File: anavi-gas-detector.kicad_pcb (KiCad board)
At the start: 2 copper layers, 74.9 x 40.6 mm, 29 parts, among them P1 CONN_01X03, U1 I2C_SENS_1, U2 I2C_SENS_1, U3 I2C_SENS_1

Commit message: anavi-gas-detector.kicad_pcb: Update labels
Improve the labels.

Signed-off-by: Leon Anavi <leon@anavi.org>
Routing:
- net +3V3: track 122.7 -> 118.7 mm, vias 2 -> 0
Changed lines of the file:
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@@
     (thickness 1.6)
     (drawings 22)
-    (tracks 187)
+    (tracks 184)
     (zones 0)
     (modules 29)
@@
       (drillshape 0)
       (scaleselection 1)
-      (outputdirectory "plots/anavi-thermometer-r1.0/"))
+      (outputdirectory "plots/anavi-gas-detector-r1.0/"))
   )
   (net 0 "")
@@
     (tags diode)
     (attr smd)
-    (fp_text reference D2 (at 0 -2.032 180) (layer F.SilkS)
+    (fp_text reference D2 (at 0 -2.1209 180) (layer F.SilkS)
       (effects (font (size 1 1) (thickness 0.15)))
     )
@@
     (tags diode)
     (attr smd)
-    (fp_text reference D3 (at 0 -1.905 180) (layer F.SilkS)
+    (fp_text reference D3 (at 0 -2.159 180) (layer F.SilkS)
       (effects (font (size 1 1) (thickness 0.15)))
     )
@@
     (tags diode)
     (attr smd)
-    (fp_text reference D4 (at 0.0635 -1.905 180) (layer F.SilkS)
+    (fp_text reference D4 (at 0 -2.1336 180) (layer F.SilkS)
       (effects (font (size 1 1) (thickness 0.15)))
     )
@@
     (tags resistor)
     (attr smd)
-    (fp_text reference R5 (at 0 -1.43) (layer F.SilkS)
+    (fp_text reference R5 (at 0.0128 1.6129) (layer F.SilkS)
       (effects (font (size 0.8 0.8) (thickness 0.1)))
     )
-    (fp_text value 68R (at 0 1.43) (layer F.Fab)
+    (fp_text value 68R (at 0 -1.4605) (layer F.Fab)
       (effects (font (size 1 1) (thickness 0.15)))
     )
@@
     (tags resistor)
     (attr smd)
-    (fp_text reference R6 (at 0 -1.43) (layer F.SilkS)
+    (fp_text reference R6 (at -0.0126 1.4986) (layer F.SilkS)
       (effects (font (size 0.8 0.8) (thickness 0.1)))
     )
-    (fp_text value 68R (at 0 1.43) (layer F.Fab)
+    (fp_text value 68R (at 0.1398 -1.3716) (layer F.Fab)
       (effects (font (size 1 1) (thickness 0.15)))
     )
@@
     (tags resistor)
     (attr smd)
-    (fp_text reference R7 (at 0 -1.43) (layer F.SilkS)
+    (fp_text reference R7 (at 0.0127 1.5494) (layer F.SilkS)
       (effects (font (size 0.8 0.8) (thickness 0.1)))
     )
-    (fp_text value 68R (at 0 1.43) (layer F.Fab)
+    (fp_text value 68R (at 0.0381 -1.3716) (layer F.Fab)
       (effects (font (size 1 1) (thickness 0.15)))
     )
@@
     (descr "Through hole straight pin header, 1x04, 2.54mm pitch, single row")
     (tags "Through hole pin header THT 1x04 2.54mm single row")
-    (fp_text reference GPIO (at 0 -2.667 270) (layer F.SilkS)
-      (effects (font (size 0.8 0.8) (thickness 0.1)))
+    (fp_text reference GPIO (at 0 -2.9718 270) (layer F.SilkS)
+      (effects (font (size 1 1) (thickness 0.2)))
     )
     (fp_text value Conn_01x04 (at 0 9.95 270) (layer F.Fab) hide
@@
     (effects (font (size 1 1) (thickness 0.2)))
   )
-  (gr_text "3 x I2C" (at 98.044 90.17 90) (layer F.SilkS)
-    (effects (font (size 1 1) (thickness 0.2)))
+  (gr_text "3 x I2C" (at 111.5822 90.297 90) (layer F.SilkS)
+    (effects (font (size 1.5 1.5) (thickness 0.25)))
   )
   (gr_line (start 69.85 71.12) (end 134.62 71.12) (angle 90) (layer Edge.Cuts) (width 0.15))
@@
   (segment (start 108.3945 90.297) (end 108.3945 91.813) (width 0.5) (layer F.Cu) (net 3))
   (segment (start 108.3945 95.5294) (end 108.3945 95.377) (width 0.5) (layer F.Cu) (net 3))
-  (via (at 80.264 101.6) (size 0.85) (drill 0.4) (layers F.Cu B.Cu) (net 3))
   (segment (start 78.283 99.568) (end 78.283 99.619) (width 0.5) (layer F.Cu) (net 3))
-  (segment (start 78.283 99.619) (end 80.264 101.6) (width 0.5) (layer F.Cu) (net 3))
-  (via (at 80.264 97.028) (size 0.85) (drill 0.4) (layers F.Cu B.Cu) (net 3))
-  (segment (start 80.264 101.6) (end 80.264 97.028) (width 0.5) (layer B.Cu) (net 3))
-  (segment (start 80.264 94.645) (end 80.899 94.01) (width 0.5) (layer F.Cu) (net 3))
-  (segment (start 80.264 97.028) (end 80.264 94.645) (width 0.5) (layer F.Cu) (net 3))
   (segment (start 80.899 84.01) (end 88.582 84.01) (width 0.5) (layer F.Cu) (net 3))
   (segment (start 88.582 84.01) (end 90.678 86.106) (width 0.5) (layer F.Cu) (net 3))
@@
   (segment (start 117.745022 81.6864) (end 122.682 76.749422) (width 0.5) (layer F.Cu) (net 3))
   (segment (start 113.2887 81.6864) (end 117.745022 81.6864) (width 0.5) (layer F.Cu) (net 3))
+  (segment (start 78.744612 99.106388) (end 78.744612 96.164388) (width 0.5) (layer F.Cu) (net 3))
+  (segment (start 78.744612 96.164388) (end 80.899 94.01) (width 0.5) (layer F.Cu) (net 3))
+  (segment (start 78.283 99.568) (end 78.744612 99.106388) (width 0.5) (layer F.Cu) (net 3))
   (segment (start 100.5635 95.969) (end 100.7745 95.758) (width 0.5) (layer F.Cu) (net 4))
   (segment (start 100.754 85.1965) (end 100.7745 85.217) (width 0.5) (layer F.Cu) (net 4))

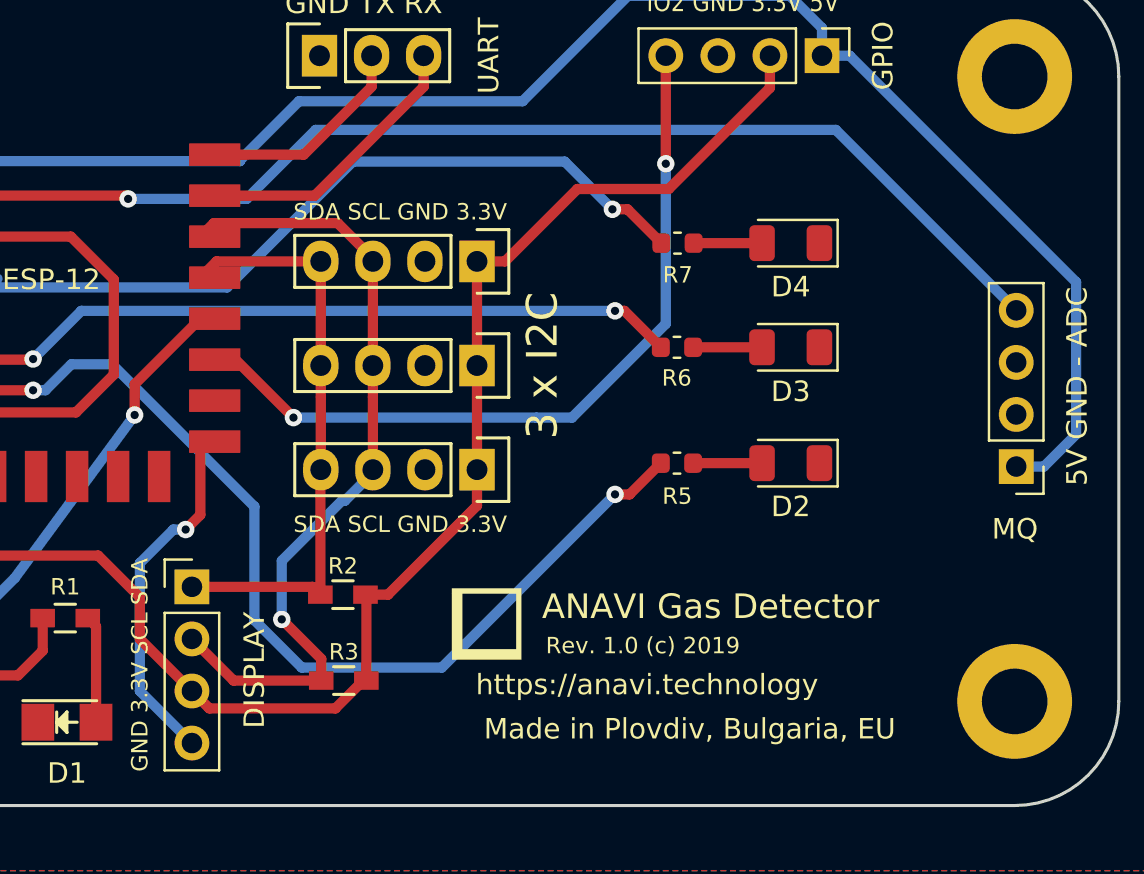
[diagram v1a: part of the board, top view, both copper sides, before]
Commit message: anavi-gas-detector.*: Add voltage dividers
Add voltage divider to measure accrately the analog
output from the external gas sensor.

Signed-off-by: Leon Anavi <leon@anavi.org>
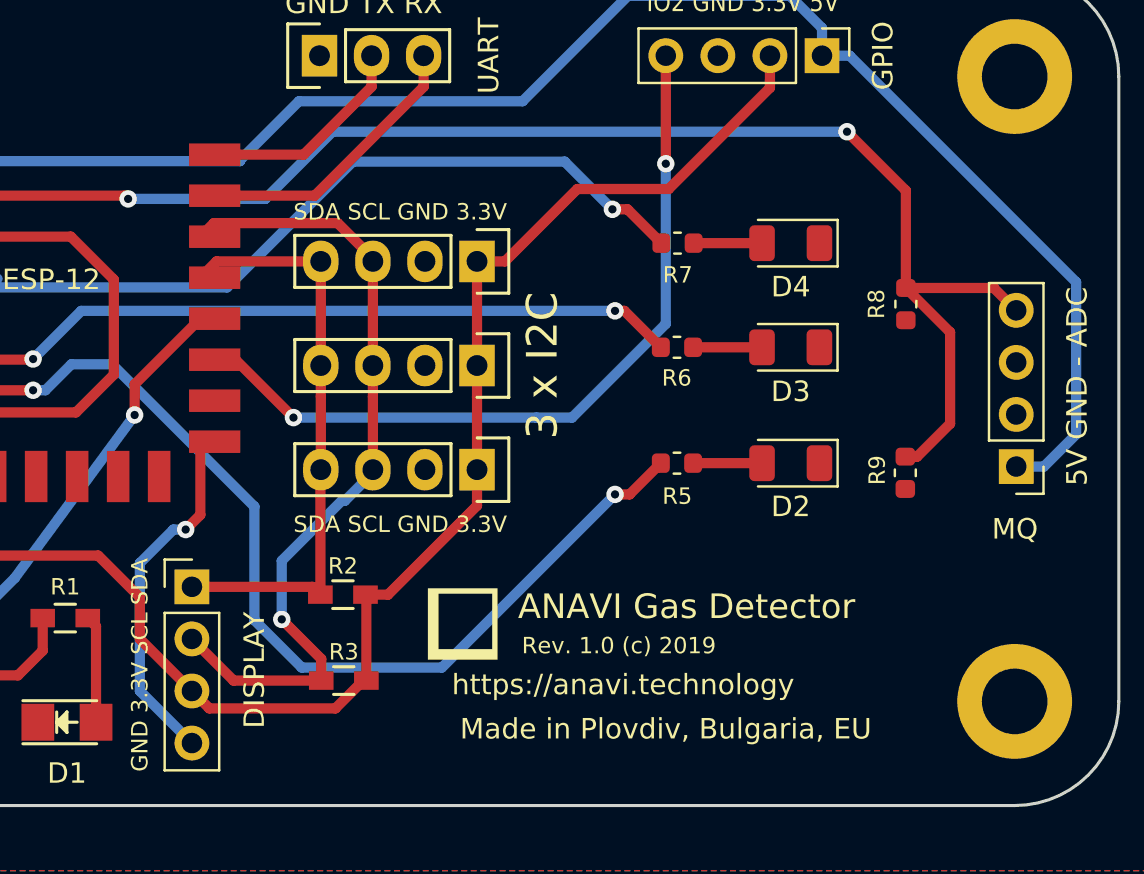
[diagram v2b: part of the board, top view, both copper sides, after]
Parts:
- added R8: 220K, Resistor_SMD:R_0603_1608Metric, F.Cu at (129.3, 87.3)
- added R9: 56K, Resistor_SMD:R_0603_1608Metric, F.Cu at (129.3, 95.5)
- moved G*** 1.17 mm to (107.7, 102.9)
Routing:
- net Net-(ESP-12-Pad2): track 58.9 -> 72.0 mm, vias 1 -> 2
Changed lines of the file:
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@@
     (thickness 1.6)
     (drawings 22)
-    (tracks 184)
+    (tracks 192)
     (zones 0)
-    (modules 29)
-    (nets 27)
+    (modules 31)
+    (nets 28)
   )
   (page A4)
@@
   (net 25 "Net-(ESP-12-Pad22)")
   (net 26 "Net-(U5-Pad3)")
+  (net 27 "Net-(R8-Pad1)")
   (net_class Default "This is the default net class."
     (clearance 0.254)
@@
     (add_net "Net-(ESP-12-Pad6)")
     (add_net "Net-(ESP-12-Pad7)")
+    (add_net "Net-(R8-Pad1)")
     (add_net "Net-(U5-Pad3)")
   )
@@
   )
   (module logo:anavi-logo (layer F.Cu)
-    (at 108.8644 102.9462)
+    (at 107.696 102.9462)
     (fp_text reference G*** (at 0 0) (layer F.SilkS) hide
       (effects (font (size 1.524 1.524) (thickness 0.3)))
@@
     )
   )
+  (module Resistor_SMD:R_0603_1608Metric (layer F.Cu)
+    (at 129.3114 87.2997 90)
+    (descr "Resistor SMD 0603 (1608 Metric), square (rectangular) end terminal, IPC_7351 nominal, (Body size source: http://www.tortai-tech.com/upload/download/2011102023233369053.pdf), generated with kicad-footprint-generator")
+    (tags resistor)
+    (attr smd)
+    (fp_text reference R8 (at 0 -1.43 90) (layer F.SilkS)
+      (effects (font (size 0.8 0.8) (thickness 0.1)))
+    )
+    (fp_text value 220K (at -0.0255 1.6002 90) (layer F.Fab)
+      (effects (font (size 1 1) (thickness 0.15)))
+    )
+    (fp_text user %R (at 0 0 90) (layer F.Fab)
+      (effects (font (size 0.4 0.4) (thickness 0.06)))
+    )
+    (fp_line (start 1.48 0.73) (end -1.48 0.73) (layer F.CrtYd) (width 0.05))
+    (fp_line (start 1.48 -0.73) (end 1.48 0.73) (layer F.CrtYd) (width 0.05))
+    (fp_line (start -1.48 -0.73) (end 1.48 -0.73) (layer F.CrtYd) (width 0.05))
+    (fp_line (start -1.48 0.73) (end -1.48 -0.73) (layer F.CrtYd) (width 0.05))
+    (fp_line (start -0.162779 0.51) (end 0.162779 0.51) (layer F.SilkS) (width 0.12))
+    (fp_line (start -0.162779 -0.51) (end 0.162779 -0.51) (layer F.SilkS) (width 0.12))
+    (fp_line (start 0.8 0.4) (end -0.8 0.4) (layer F.Fab) (width 0.1))
+    (fp_line (start 0.8 -0.4) (end 0.8 0.4) (layer F.Fab) (width 0.1))
+    (fp_line (start -0.8 -0.4) (end 0.8 -0.4) (layer F.Fab) (width 0.1))
+    (fp_line (start -0.8 0.4) (end -0.8 -0.4) (layer F.Fab) (width 0.1))
+    (pad 2 smd roundrect (at 0.7875 0 90) (size 0.875 0.95) (layers F.Cu F.Paste F.Mask) (roundrect_rratio 0.25)
+      (net 17 "Net-(ESP-12-Pad2)"))
+    (pad 1 smd roundrect (at -0.7875 0 90) (size 0.875 0.95) (layers F.Cu F.Paste F.Mask) (roundrect_rratio 0.25)
+      (net 27 "Net-(R8-Pad1)"))
+    (model ${KISYS3DMOD}/Resistor_SMD.3dshapes/R_0603_1608Metric.wrl
+      (at (xyz 0 0 0))
+      (scale (xyz 1 1 1))
+      (rotate (xyz 0 0 0))
+    )
+  )
+  (module Resistor_SMD:R_0603_1608Metric (layer F.Cu)
+    (at 129.286 95.5295 270)
+    (descr "Resistor SMD 0603 (1608 Metric), square (rectangular) end terminal, IPC_7351 nominal, (Body size source: http://www.tortai-tech.com/upload/download/2011102023233369053.pdf), generated with kicad-footprint-generator")
+    (tags resistor)
+    (attr smd)
+    (fp_text reference R9 (at -0.1271 1.3716 270) (layer F.SilkS)
+      (effects (font (size 0.8 0.8) (thickness 0.1)))
+    )
+    (fp_text value 56K (at 0.0253 -1.5748 270) (layer F.Fab)
+      (effects (font (size 1 1) (thickness 0.15)))
+    )
+    (fp_line (start -0.8 0.4) (end -0.8 -0.4) (layer F.Fab) (width 0.1))
+    (fp_line (start -0.8 -0.4) (end 0.8 -0.4) (layer F.Fab) (width 0.1))
+    (fp_line (start 0.8 -0.4) (end 0.8 0.4) (layer F.Fab) (width 0.1))
+    (fp_line (start 0.8 0.4) (end -0.8 0.4) (layer F.Fab) (width 0.1))
+    (fp_line (start -0.162779 -0.51) (end 0.162779 -0.51) (layer F.SilkS) (width 0.12))
+    (fp_line (start -0.162779 0.51) (end 0.162779 0.51) (layer F.SilkS) (width 0.12))
+    (fp_line (start -1.48 0.73) (end -1.48 -0.73) (layer F.CrtYd) (width 0.05))
+    (fp_line (start -1.48 -0.73) (end 1.48 -0.73) (layer F.CrtYd) (width 0.05))
+    (fp_line (start 1.48 -0.73) (end 1.48 0.73) (layer F.CrtYd) (width 0.05))
+    (fp_line (start 1.48 0.73) (end -1.48 0.73) (layer F.CrtYd) (width 0.05))
+    (fp_text user %R (at 0 0 270) (layer F.Fab)
+      (effects (font (size 0.4 0.4) (thickness 0.06)))
+    )
+    (pad 1 smd roundrect (at -0.7875 0 270) (size 0.875 0.95) (layers F.Cu F.Paste F.Mask) (roundrect_rratio 0.25)
+      (net 17 "Net-(ESP-12-Pad2)"))
+    (pad 2 smd roundrect (at 0.7875 0 270) (size 0.875 0.95) (layers F.Cu F.Paste F.Mask) (roundrect_rratio 0.25)
+      (net 2 GND))
+    (model ${KISYS3DMOD}/Resistor_SMD.3dshapes/R_0603_1608Metric.wrl
+      (at (xyz 0 0 0))
+      (scale (xyz 1 1 1))
+      (rotate (xyz 0 0 0))
+    )
+  )
   (gr_text "IO2 GND 3.3V 5V" (at 121.3612 72.5932) (layer F.SilkS)
     (effects (font (size 0.9 0.8) (thickness 0.15)))
@@
     (effects (font (size 1 1) (thickness 0.15)))
   )
-  (gr_text "Made in Plovdiv, Bulgaria, EU" (at 118.7704 108.0262) (layer F.SilkS)
+  (gr_text "Made in Plovdiv, Bulgaria, EU" (at 117.602 108.0262) (layer F.SilkS)
     (effects (font (size 1 1) (thickness 0.2)))
   )
-  (gr_text https://anavi.technology (at 116.6876 105.8672) (layer F.SilkS)
+  (gr_text https://anavi.technology (at 115.5192 105.8672) (layer F.SilkS)
     (effects (font (size 1 1) (thickness 0.15)))
   )
-  (gr_text "Rev. 1.0 (c) 2019" (at 116.4844 103.9622) (layer F.SilkS)
+  (gr_text "Rev. 1.0 (c) 2019" (at 115.316 103.9622) (layer F.SilkS)
     (effects (font (size 0.8 0.8) (thickness 0.15)))
   )
-  (gr_text "ANAVI Gas Detector" (at 119.7864 102.0572) (layer F.SilkS)
+  (gr_text "ANAVI Gas Detector" (at 118.618 102.0572) (layer F.SilkS)
     (effects (font (size 1.2 1.2) (thickness 0.25)))
   )
@@
   (segment (start 80.899 82.01) (end 91.2175 82.01) (width 0.5) (layer F.Cu) (net 17))
   (segment (start 91.2175 82.01) (end 91.3765 82.169) (width 0.5) (layer F.Cu) (net 17))
-  (segment (start 125.8951 78.8035) (end 134.6962 87.6046) (width 0.5) (layer B.Cu) (net 17))
-  (segment (start 100.5205 78.8035) (end 125.8951 78.8035) (width 0.5) (layer B.Cu) (net 17))
-  (segment (start 91.3765 82.169) (end 97.155 82.169) (width 0.5) (layer B.Cu) (net 17))
-  (segment (start 97.155 82.169) (end 100.5205 78.8035) (width 0.5) (layer B.Cu) (net 17))
+  (segment (start 91.3765 82.169) (end 98.0694 82.169) (width 0.5) (layer B.Cu) (net 17))
+  (via (at 126.4412 78.8924) (size 0.85) (drill 0.4) (layers F.Cu B.Cu) (net 17))
+  (segment (start 98.0694 82.169) (end 101.346 78.8924) (width 0.5) (layer B.Cu) (net 17))
+  (segment (start 101.346 78.8924) (end 126.4412 78.8924) (width 0.5) (layer B.Cu) (net 17))
+  (segment (start 129.3114 81.7626) (end 129.3114 86.5122) (width 0.5) (layer F.Cu) (net 17))
+  (segment (start 126.4412 78.8924) (end 129.3114 81.7626) (width 0.5) (layer F.Cu) (net 17))
+  (segment (start 133.6038 86.5122) (end 134.6962 87.6046) (width 0.5) (layer F.Cu) (net 17))
+  (segment (start 129.3114 86.5122) (end 133.6038 86.5122) (width 0.5) (layer F.Cu) (net 17))
+  (segment (start 129.861 94.742) (end 131.4704 93.1326) (width 0.5) (layer F.Cu) (net 17))
+  (segment (start 129.286 94.742) (end 129.861 94.742) (width 0.5) (layer F.Cu) (net 17))
+  (segment (start 131.4704 88.6712) (end 129.3114 86.5122) (width 0.5) (layer F.Cu) (net 17))
+  (segment (start 131.4704 93.1326) (end 131.4704 88.6712) (width 0.5) (layer F.Cu) (net 17))
   (via (at 84.582 86.487) (size 0.85) (drill 0.4) (layers F.Cu B.Cu) (net 18))
   (segment (start 80.899 88.01) (end 83.059 88.01) (width 0.5) (layer F.Cu) (net 18))

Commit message: anavi-gas-detector.kicad_pcb: Rev 1.1
Update the revision number to 1.1.

Signed-off-by: Leon Anavi <leon@anavi.org>
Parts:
- moved G*** 0.25 mm to (108.0, 102.9)
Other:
- board text added: ">"
- board text added: "Rev. 1.1 (c) 2019"
- board text removed: "Rev. 1.0 (c) 2019"
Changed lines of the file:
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@@
   (general
     (thickness 1.6)
-    (drawings 22)
+    (drawings 25)
     (tracks 192)
     (zones 0)
@@
       (drillshape 0)
       (scaleselection 1)
-      (outputdirectory "plots/anavi-gas-detector-r1.0/"))
+      (outputdirectory "plots/anavi-gas-detector-r1.1/"))
   )
   (net 0 "")
@@
   )
   (module logo:anavi-logo (layer F.Cu)
-    (at 107.696 102.9462)
+    (at 107.95 102.9462)
     (fp_text reference G*** (at 0 0) (layer F.SilkS) hide
       (effects (font (size 1.524 1.524) (thickness 0.3)))
@@
     )
   )
+  (gr_text > (at 123.7488 95.0468) (layer F.SilkS)
+    (effects (font (size 1 1) (thickness 0.1)))
+  )
+  (gr_text > (at 123.7488 89.3572) (layer F.SilkS)
+    (effects (font (size 1 1) (thickness 0.1)))
+  )
+  (gr_text > (at 123.7488 84.2264) (layer F.SilkS)
+    (effects (font (size 1 1) (thickness 0.1)))
+  )
   (gr_text "IO2 GND 3.3V 5V" (at 121.3612 72.5932) (layer F.SilkS)
     (effects (font (size 0.9 0.8) (thickness 0.15)))
@@
     (effects (font (size 1 1) (thickness 0.15)))
   )
-  (gr_text "Made in Plovdiv, Bulgaria, EU" (at 117.602 108.0262) (layer F.SilkS)
+  (gr_text "Made in Plovdiv, Bulgaria, EU" (at 117.856 108.0262) (layer F.SilkS)
     (effects (font (size 1 1) (thickness 0.2)))
   )
-  (gr_text https://anavi.technology (at 115.5192 105.8672) (layer F.SilkS)
+  (gr_text https://anavi.technology (at 115.7732 105.8672) (layer F.SilkS)
     (effects (font (size 1 1) (thickness 0.15)))
   )
-  (gr_text "Rev. 1.0 (c) 2019" (at 115.316 103.9622) (layer F.SilkS)
+  (gr_text "Rev. 1.1 (c) 2019" (at 115.57 103.9622) (layer F.SilkS)
     (effects (font (size 0.8 0.8) (thickness 0.15)))
   )
-  (gr_text "ANAVI Gas Detector" (at 118.618 102.0572) (layer F.SilkS)
+  (gr_text "ANAVI Gas Detector" (at 118.872 102.0572) (layer F.SilkS)
     (effects (font (size 1.2 1.2) (thickness 0.25)))
   )

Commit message: anavi-gas-detector.kicad_pcb: Assembly diagram
Update assembly instructions.

Signed-off-by: Leon Anavi <leon@anavi.org>
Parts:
- D2: value LED -> KP-3216SGC
- D3: value LED -> KP-3216YC
- D4: value LED -> KP-3216EC
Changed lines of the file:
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@@
       (effects (font (size 0.8 0.8) (thickness 0.15)))
     )
-    (fp_text value 68R (at 0.0205 0.0635) (layer F.Fab)
+    (fp_text value 68R (at 0.1348 1.7272) (layer F.Fab)
       (effects (font (size 1 1) (thickness 0.15)))
     )
@@
       (effects (font (size 1 1) (thickness 0.15)))
     )
-    (fp_text value LED (at 0 1.82 180) (layer F.Fab)
-      (effects (font (size 1 1) (thickness 0.15)))
+    (fp_text value KP-3216SGC (at 0 1.82 180) (layer F.Fab)
+      (effects (font (size 0.8 0.6) (thickness 0.15)))
     )
     (fp_line (start 1.6 -0.8) (end -1.2 -0.8) (layer F.Fab) (width 0.1))
@@
       (effects (font (size 1 1) (thickness 0.15)))
     )
-    (fp_text value LED (at 0 1.82 180) (layer F.Fab)
-      (effects (font (size 1 1) (thickness 0.15)))
+    (fp_text value KP-3216YC (at 0 1.82 180) (layer F.Fab)
+      (effects (font (size 0.8 0.6) (thickness 0.15)))
     )
     (fp_text user %R (at 0 0 180) (layer F.Fab)
@@
       (effects (font (size 1 1) (thickness 0.15)))
     )
-    (fp_text value LED (at 0 1.82 180) (layer F.Fab)
-      (effects (font (size 1 1) (thickness 0.15)))
+    (fp_text value KP-3216EC (at 0 1.82 180) (layer F.Fab)
+      (effects (font (size 0.8 0.6) (thickness 0.15)))
     )
     (fp_line (start 1.6 -0.8) (end -1.2 -0.8) (layer F.Fab) (width 0.1))
